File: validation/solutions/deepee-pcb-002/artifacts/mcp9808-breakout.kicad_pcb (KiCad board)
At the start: 2 copper layers, 18 x 15 mm, 6 parts, among them J1 Conn_01x05, U1 MCP9808T-E/MS

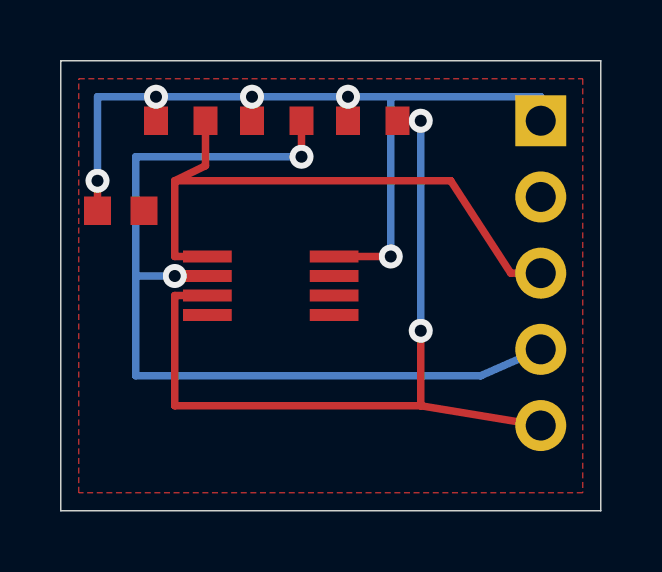
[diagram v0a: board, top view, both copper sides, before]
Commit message: feat: prepare the 48-task benchmark suite
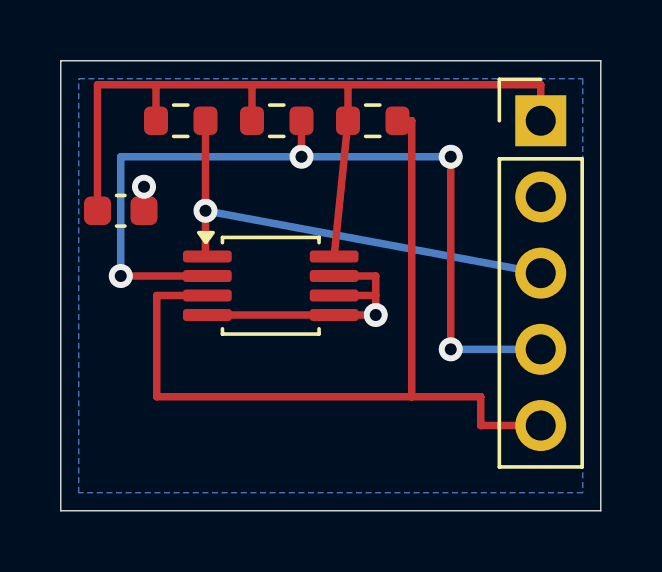
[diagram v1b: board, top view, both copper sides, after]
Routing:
- net GND: track 0.00 -> 10.5 mm, vias 0 -> 2
- net SDA: track 20.1 -> 16.0 mm, vias 0 -> 1
- net SCL: track 30.1 -> 28.5 mm, vias 2 -> 4
- net ALERT: track 27.3 -> 28.5 mm, vias 2 -> 0
- net 3V3: track 29.0 -> 28.3 mm, vias 5 -> 0
- added copper zone on B.Cu, net GND
- removed copper zone on F.Cu, net GND
